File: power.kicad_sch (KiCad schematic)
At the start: 17 parts

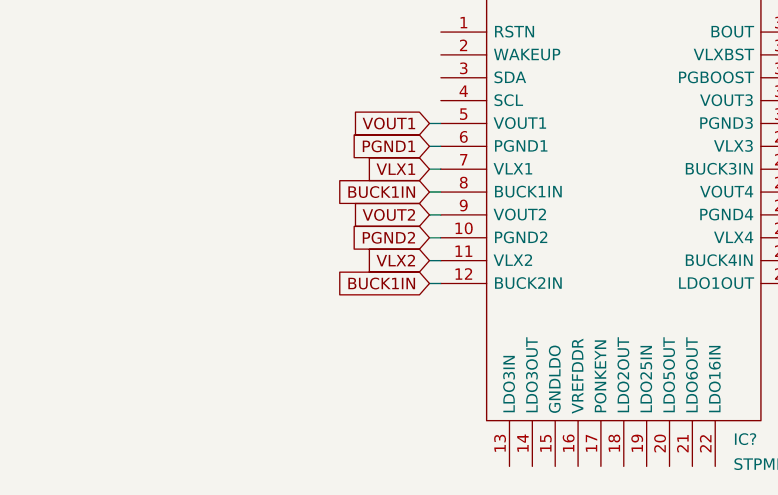
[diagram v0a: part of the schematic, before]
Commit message: Change Symbols / Footprintst to local library
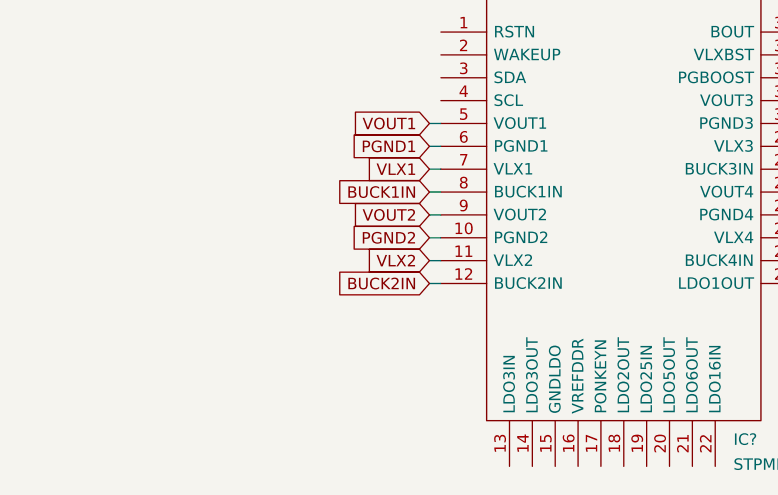
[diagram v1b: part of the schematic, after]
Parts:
- removed IC?: STPMIC1EPQR, QFN40P500X600X80-45N-D, symbol SamacSys_Parts:STPMIC1EPQR
- added IC?: STPMIC1EPQR, QFN40P500X600X80-45N-D, symbol mp1lib:STPMIC1EPQR
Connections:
- net 3V3: now also IC?.27 (VOUT4)
- net GND: now also IC?.10 (PGND2), IC?.26 (PGND4), IC?.30 (PGND3), IC?.6 (PGND1)
- net VDD: now also IC?.31 (VOUT3)
- net VDD_Core: now also IC?.5 (VOUT1)
- net VDD_DDR: now also IC?.9 (VOUT2)
- net VLX1: now also IC?.7 (VLX1)
- net VLX2: now also IC?.11 (VLX2)
- net VLX3: now also IC?.29 (VLX3)
- net VLX4: now also IC?.25 (VLX4)
- net VSS: now also IC?.12 (BUCK2IN), IC?.24 (BUCK4IN), IC?.28 (BUCK3IN), IC?.8 (BUCK1IN)
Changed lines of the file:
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@@
     )
   )
-  (global_label "BUCK1IN" (shape input) (at 66.04 77.47 180) (fields_autoplaced)
+  (global_label "BUCK2IN" (shape input) (at 66.04 77.47 180) (fields_autoplaced)
     (effects (font (size 1.27 1.27)) (justify right))
     (property "Intersheet References" "${INTERSHEET_REFS}" (id 0) (at 55.3417 77.3906 0)
@@
     (pin "1")
   )
-  (symbol (lib_id "SamacSys_Parts:STPMIC1EPQR") (at 67.31 49.53 0) (unit 1)
+  (symbol (lib_id "mp1lib:STPMIC1EPQR") (at 67.31 49.53 0) (unit 1)
     (in_bom yes) (on_board yes) (fields_autoplaced)
     (property "Reference" "IC?" (id 0) (at 99.8094 94.8087 0)

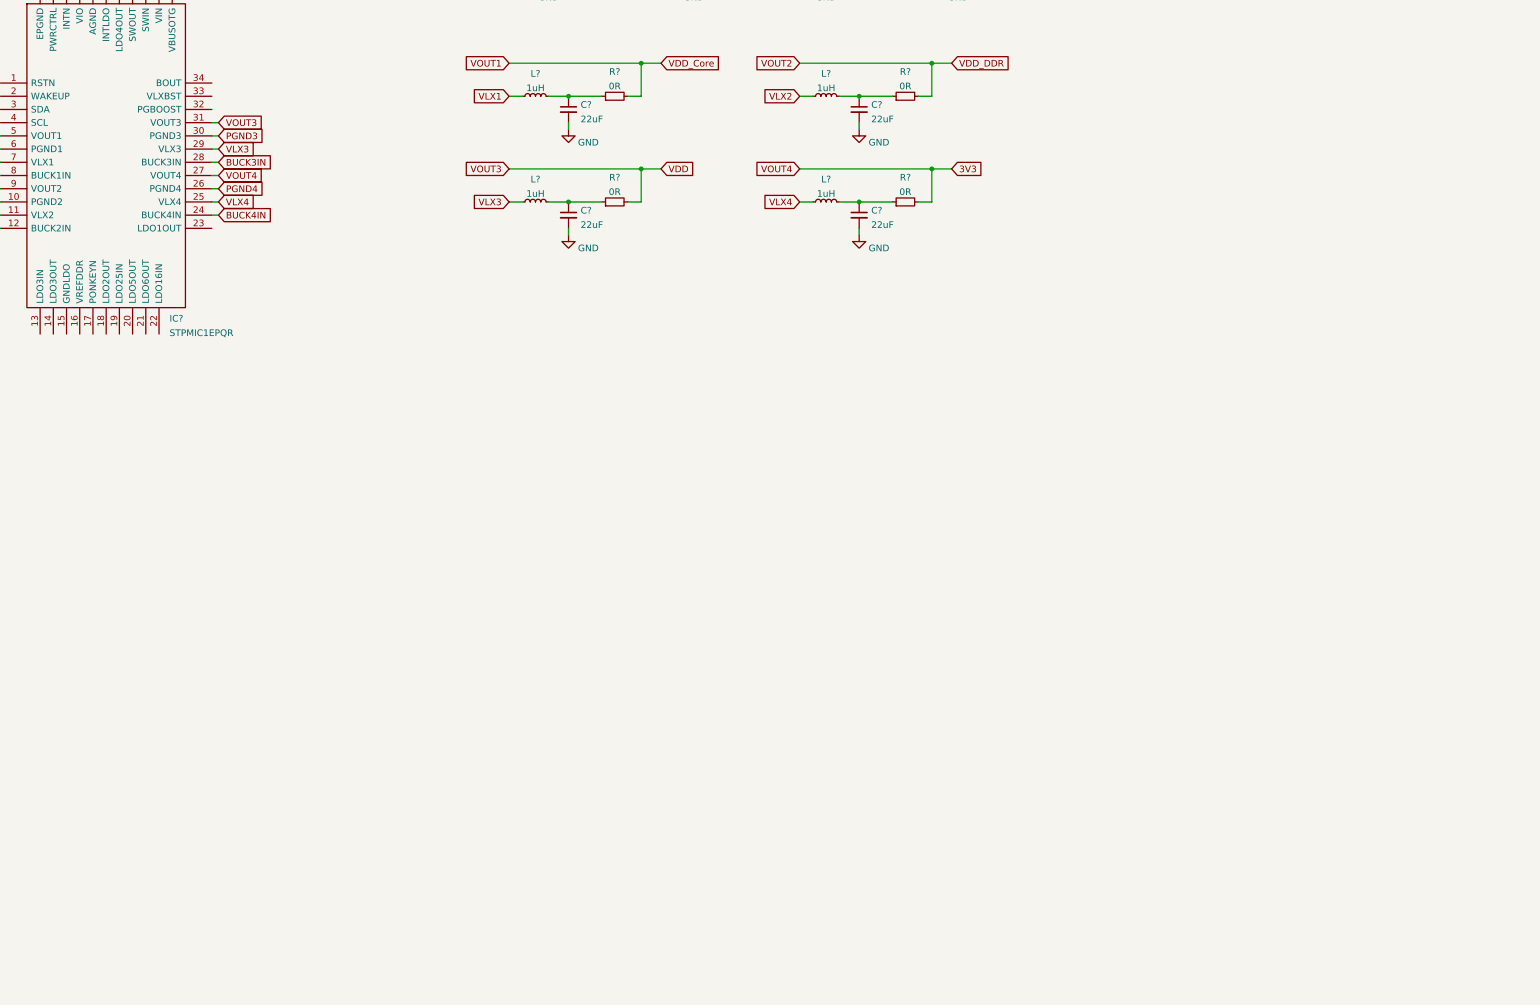
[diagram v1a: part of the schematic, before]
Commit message: Modified STM32 Symbol: - moved supply in seperate unit
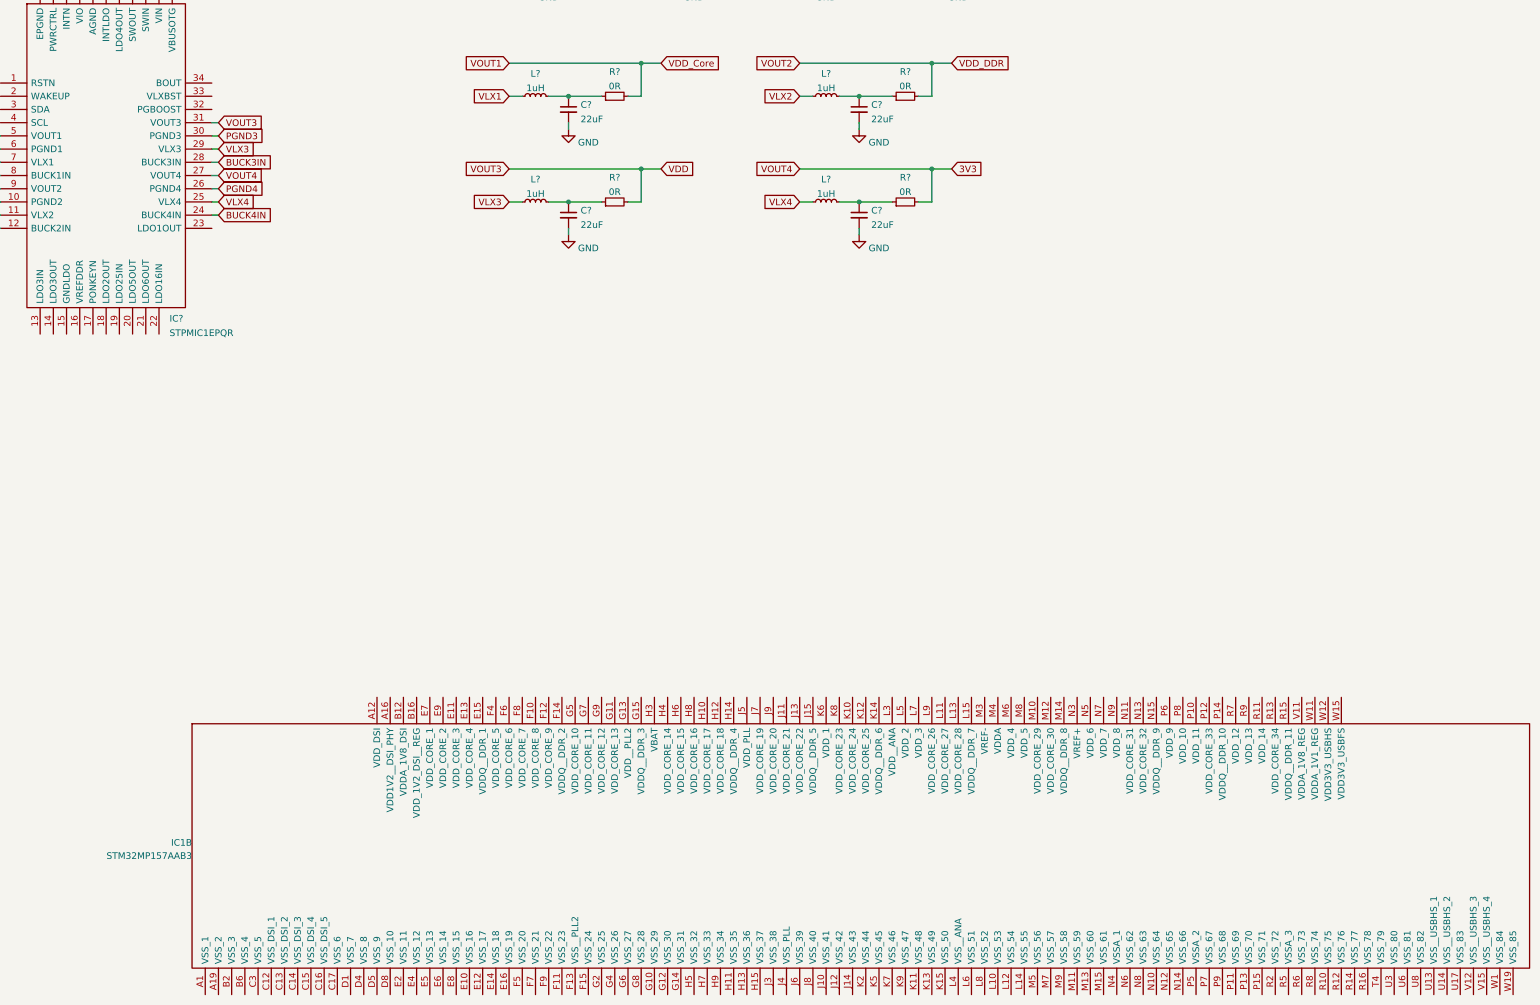
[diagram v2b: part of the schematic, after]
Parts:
- added IC1: STM32MP157AAB3, ARMband:BGA354C80P19X19_1600X1600X129, symbol ARMband:STM32MP157AAB3_(modified)

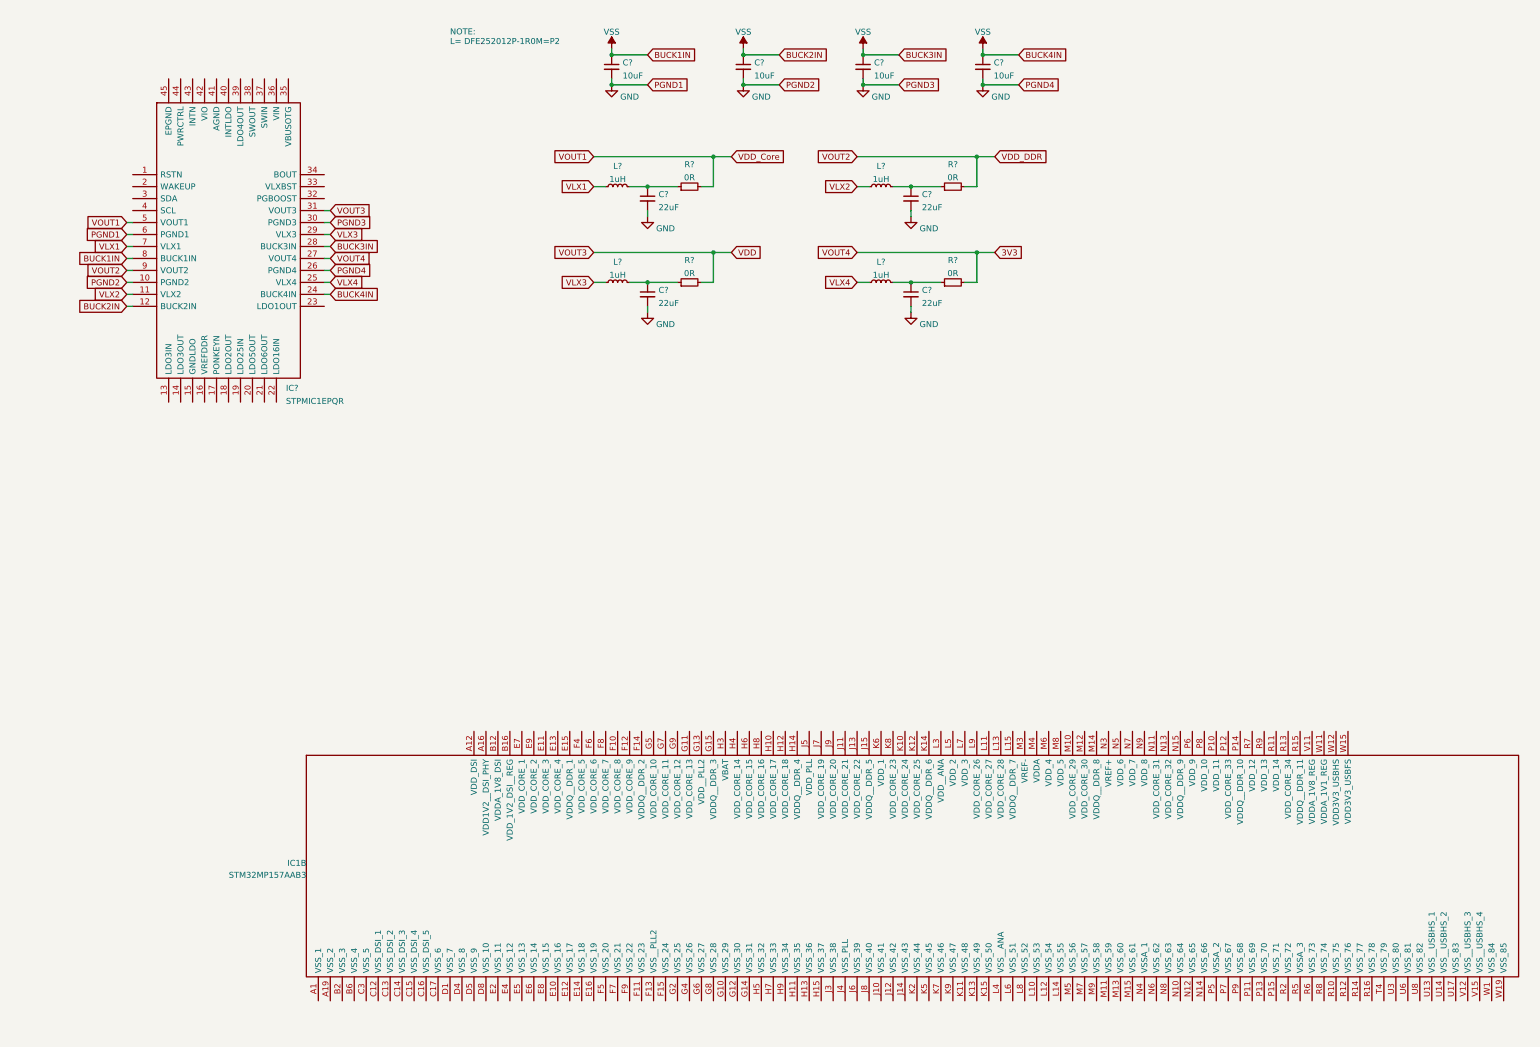
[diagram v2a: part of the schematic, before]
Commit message: Connected power rails to mp1
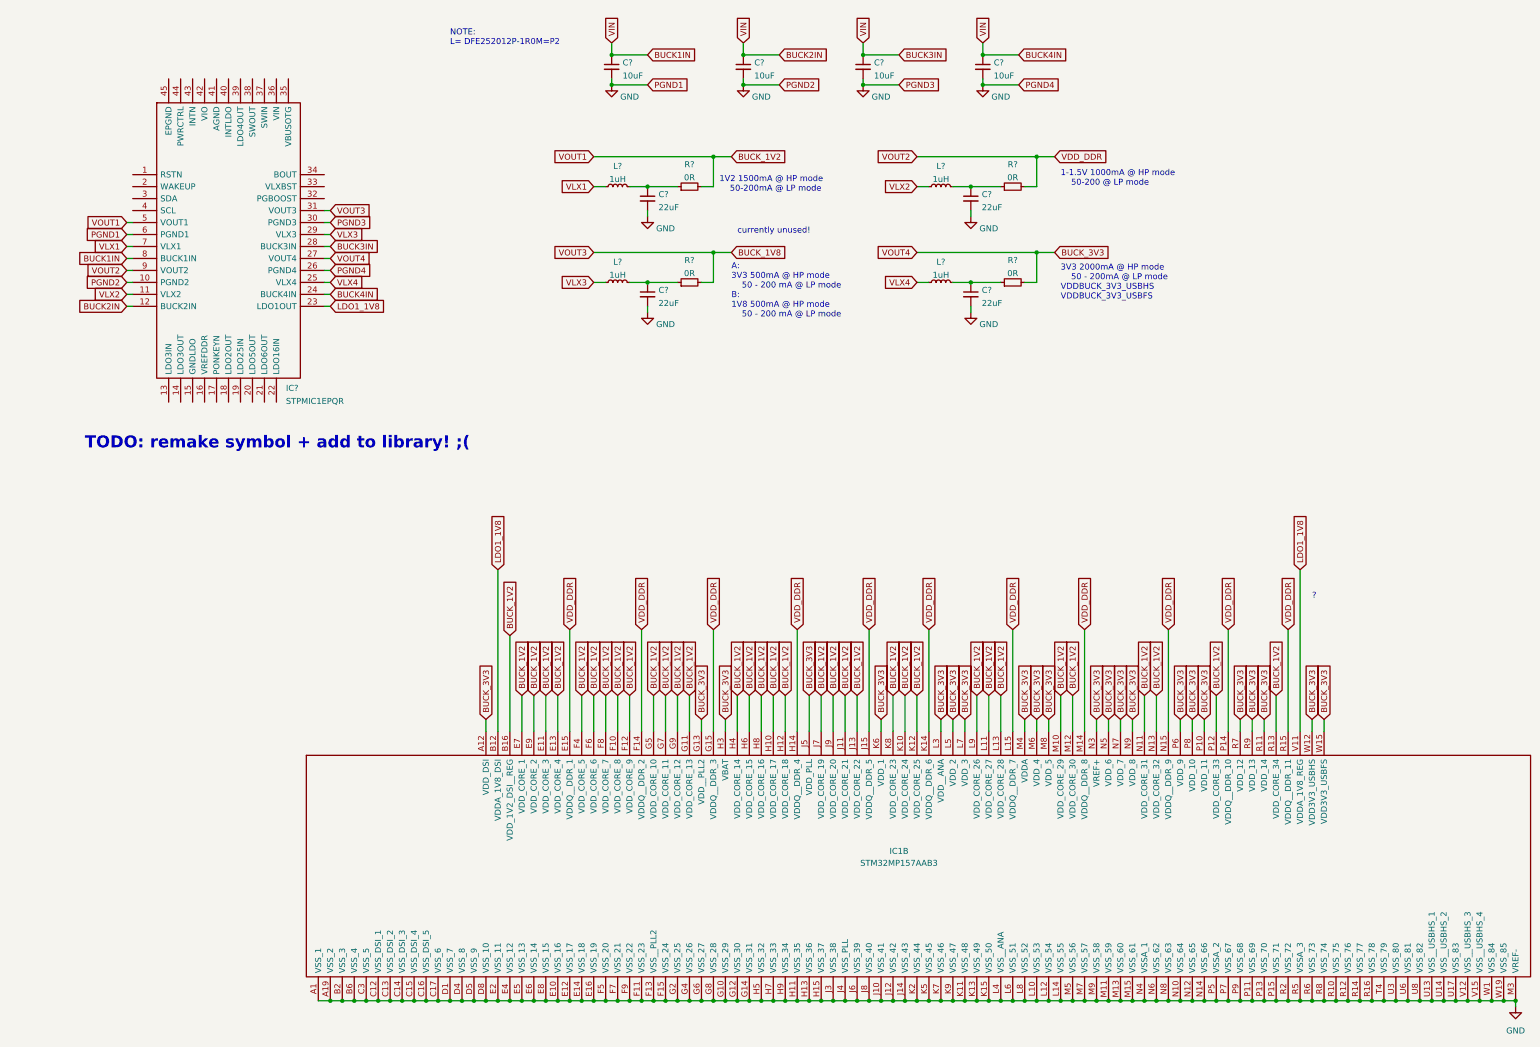
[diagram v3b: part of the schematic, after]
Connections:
- net 3V3 is gone; now on net BUCK_3V3: IC?.27 (VOUT4), R?.2
- net VDD_Core is gone; now on net BUCK_1V2: IC?.5 (VOUT1), R?.2
- net GND: now also IC1.A1 (VSS_1), IC1.A19 (VSS_2), IC1.B2 (VSS_3), IC1.B6 (VSS_4), IC1.C12 (VSS_DSI_1), IC1.C13 (VSS_DSI_2), IC1.C14 (VSS_DSI_3), IC1.C15 (VSS_DSI_4), IC1.C16 (VSS_DSI_5), IC1.C17 (VSS_6), IC1.C3 (VSS_5), IC1.D1 (VSS_7), IC1.D4 (VSS_8), IC1.D5 (VSS_9), IC1.D8 (VSS_10), IC1.E10 (VSS_16), IC1.E12 (VSS_17), IC1.E14 (VSS_18), IC1.E16 (VSS_19), IC1.E2 (VSS_11), IC1.E4 (VSS_12), IC1.E5 (VSS_13), IC1.E6 (VSS_14), IC1.E8 (VSS_15), IC1.F11 (VSS_23), IC1.F13 (VSS__PLL2), IC1.F15 (VSS_24), IC1.F5 (VSS_20), IC1.F7 (VSS_21), IC1.F9 (VSS_22), IC1.G10 (VSS_29), IC1.G12 (VSS_30), IC1.G14 (VSS_31), IC1.G2 (VSS_25), IC1.G4 (VSS_26), IC1.G6 (VSS_27), IC1.G8 (VSS_28), IC1.H11 (VSS_35), IC1.H13 (VSS_36), IC1.H15 (VSS_37), IC1.H5 (VSS_32), IC1.H7 (VSS_33), IC1.H9 (VSS_34), IC1.J10 (VSS_41), IC1.J12 (VSS_42), IC1.J14 (VSS_43), IC1.J3 (VSS_38), IC1.J4 (VSS_PLL), IC1.J6 (VSS_39), IC1.J8 (VSS_40), IC1.K11 (VSS_48), IC1.K13 (VSS_49), IC1.K15 (VSS_50), IC1.K2 (VSS_44), IC1.K5 (VSS_45), IC1.K7 (VSS_46), IC1.K9 (VSS_47), IC1.L10 (VSS_53), IC1.L12 (VSS_54), IC1.L14 (VSS_55), IC1.L4 (VSS__ANA), IC1.L6 (VSS_51), IC1.L8 (VSS_52), IC1.M11 (VSS_59), IC1.M13 (VSS_60), IC1.M15 (VSS_61), IC1.M3 (VREF-), IC1.M5 (VSS_56), IC1.M7 (VSS_57), IC1.M9 (VSS_58), IC1.N10 (VSS_64), IC1.N12 (VSS_65), IC1.N14 (VSS_66), IC1.N4 (VSSA_1), IC1.N6 (VSS_62), IC1.N8 (VSS_63), IC1.P11 (VSS_69), IC1.P13 (VSS_70), IC1.P15 (VSS_71), IC1.P5 (VSSA_2), IC1.P7 (VSS_67), IC1.P9 (VSS_68), IC1.R10 (VSS_75), IC1.R12 (VSS_76), IC1.R14 (VSS_77), IC1.R16 (VSS_78), IC1.R2 (VSS_72), IC1.R5 (VSSA_3), IC1.R6 (VSS_73), IC1.R8 (VSS_74), IC1.T4 (VSS_79), IC1.U13 (VSS__USBHS_1), IC1.U14 (VSS__USBHS_2), IC1.U17 (VSS_83), IC1.U3 (VSS_80), IC1.U6 (VSS_81), IC1.U8 (VSS_82), IC1.V12 (VSS__USBHS_3), IC1.V15 (VSS__USBHS_4), IC1.W1 (VSS_84), IC1.W19 (VSS_85)
- net VDD_DDR: now also IC1.E15 (VDDQ__DDR_1), IC1.F14 (VDDQ__DDR_2), IC1.G15 (VDDQ__DDR_3), IC1.H14 (VDDQ__DDR_4), IC1.J15 (VDDQ__DDR_5), IC1.K14 (VDDQ__DDR_6), IC1.L15 (VDDQ__DDR_7), IC1.M14 (VDDQ__DDR_8), IC1.N15 (VDDQ__DDR_9), IC1.P14 (VDDQ__DDR_10), IC1.R15 (VDDQ__DDR_11)
- net BUCK_3V3: now reaches IC1.A12 (VDD_DSI)
- net BUCK_3V3: now also IC1.G13 (VDD__PLL2), IC1.H3 (VBAT), IC1.J5 (VDD_PLL), IC1.K6 (VDD_1), IC1.L3 (VDD__ANA), IC1.L5 (VDD_2), IC1.L7 (VDD_3), IC1.M4 (VDDA), IC1.M6 (VDD_4), IC1.M8 (VDD_5), IC1.N3 (VREF+), IC1.N5 (VDD_6), IC1.N7 (VDD_7), IC1.N9 (VDD_8), IC1.P10 (VDD_11), IC1.P6 (VDD_9), IC1.P8 (VDD_10), IC1.R11 (VDD_14), IC1.R7 (VDD_12), IC1.R9 (VDD_13), IC1.W12 (VDD3V3_USBHS), IC1.W15 (VDD3V3_USBFS)
- net LDO1_1V8: now reaches IC1.B12 (VDDA_1V8_DSI)
- net LDO1_1V8: now also IC1.V11 (VDDA_1V8_REG), IC?.23 (LDO1OUT)
- net BUCK_1V2: now reaches IC1.B16 (VDD_1V2_DSI__REG)
- net BUCK_1V2: now also IC1.E11 (VDD_CORE_3), IC1.E13 (VDD_CORE_4), IC1.E7 (VDD_CORE_1), IC1.E9 (VDD_CORE_2), IC1.F10 (VDD_CORE_8), IC1.F12 (VDD_CORE_9), IC1.F4 (VDD_CORE_5), IC1.F6 (VDD_CORE_6), IC1.F8 (VDD_CORE_7), IC1.G11 (VDD_CORE_13), IC1.G5 (VDD_CORE_10), IC1.G7 (VDD_CORE_11), IC1.G9 (VDD_CORE_12), IC1.H10 (VDD_CORE_17), IC1.H12 (VDD_CORE_18), IC1.H4 (VDD_CORE_14), IC1.H6 (VDD_CORE_15), IC1.H8 (VDD_CORE_16), IC1.J11 (VDD_CORE_21), IC1.J13 (VDD_CORE_22), IC1.J7 (VDD_CORE_19), IC1.J9 (VDD_CORE_20), IC1.K10 (VDD_CORE_24), IC1.K12 (VDD_CORE_25), IC1.K8 (VDD_CORE_23), IC1.L11 (VDD_CORE_27), IC1.L13 (VDD_CORE_28), IC1.L9 (VDD_CORE_26), IC1.M10 (VDD_CORE_29), IC1.M12 (VDD_CORE_30), IC1.N11 (VDD_CORE_31), IC1.N13 (VDD_CORE_32), IC1.P12 (VDD_CORE_33), IC1.R13 (VDD_CORE_34)
- net VDD renamed BUCK_1V8
- net VSS renamed BUCK1IN
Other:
- note added: "1-1.5V 1000mA @ HP mode 50-200 @ LP mode"
- note added: "1V2 1500mA @ HP mode 50-200mA @ LP mode"
- note added: "3V3 2000mA @ HP mode 50 - 200mA @ LP mode VDDBUCK_3V3_USBHS VDDBUCK_3V3_USBFS"
- note added: "?"
- note added: "A: 3V3 500mA @ HP mode 50 - 200 mA @ LP mode B: 1V8 500mA @ HP mode 50 - 200 mA @ LP mode"
- note added: "TODO: remake symbol + add to library! ;("
- note added: "currently unused!"
- moved on the sheet: C?, L?, R?

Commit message: added VREV_DDR
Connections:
- net VREF_DDR: now reaches IC?.16 (VREFDDR)
- net VREF_DDR: now also IC1.W16 (DDR_VREF)
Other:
- note removed: "?"
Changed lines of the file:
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@@
+    (stroke (width 0) (type default))
+  )
+  (wire (pts (xy 322.58 153.67) (xy 322.58 167.64))
     (stroke (width 0) (type default))
   )
@@
   )
   (wire (pts (xy 144.78 133.35) (xy 144.78 167.64))
+    (stroke (width 0) (type default))
+  )
+  (wire (pts (xy 82.55 97.79) (xy 82.55 100.33))
     (stroke (width 0) (type default))
   )
@@
     (effects (font (size 1.27 1.27)) (justify left bottom))
   )
-  (text "TODO: remake symbol + add to library! ;(" (at 57.15 107.95 0)
+  (text "TODO: remake symbol + add to library! ;(" (at 57.15 123.19 0)
     (effects (font (face "Yu Gothic UI") (size 2.54 2.54) (thickness 0.508) bold (color 255 0 6 1)) (justify left bottom))
   )
@@
   )
   (text "1V2 1500mA @ HP mode\n    50-200mA @ LP mode" (at 191.77 53.34 0)
-    (effects (font (size 1.27 1.27)) (justify left bottom))
-  )
-  (text "?" (at 317.5 139.7 0)
     (effects (font (size 1.27 1.27)) (justify left bottom))
   )
@@
     (effects (font (size 1.27 1.27)) (justify left))
     (property "Intersheetrefs" "${INTERSHEET_REFS}" (at 307.34 158.6866 90)
+      (effects (font (size 1.27 1.27)) (justify left) hide)
+    )
+  )
+  (global_label "VREF_DDR" (shape input) (at 82.55 100.33 270) (fields_autoplaced)
+    (effects (font (size 1.27 1.27)) (justify right))
+    (property "Intersheetrefs" "${INTERSHEET_REFS}" (at 82.55 112.6096 90)
+      (effects (font (size 1.27 1.27)) (justify right) hide)
+    )
+  )
+  (global_label "VREF_DDR" (shape input) (at 322.58 153.67 90) (fields_autoplaced)
+    (effects (font (size 1.27 1.27)) (justify left))
+    (property "Intersheetrefs" "${INTERSHEET_REFS}" (at 322.58 141.3904 90)
       (effects (font (size 1.27 1.27)) (justify left) hide)
     )
@@
     (pin "W13")
     (pin "W14")
-    (pin "W16")
     (pin "W17")
     (pin "W18")
@@
     (pin "W12")
     (pin "W15")
+    (pin "W16")
     (pin "W19")
     (instances
